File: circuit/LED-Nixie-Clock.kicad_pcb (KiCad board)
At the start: 2 copper layers, 214.6 x 43.2 mm, 197 parts, among them J1 USB Micro, J2 Debug, J3 Boot, SW1 Reset, U1 MCP1700-3302E_SOT23, U2 STM32F103C8Tx, Y1 8MHz, Y2 32.768kHz

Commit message: Improve silk layer labels
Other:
- board text added: "CR2032"
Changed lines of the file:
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@@
   (general
     (thickness 1.6)
-    (drawings 257)
+    (drawings 258)
     (tracks 1823)
     (zones 0)
@@
     (tags "SPST button tactile switch")
     (attr smd)
-    (fp_text reference SW1 (at 0 -2.54 180) (layer B.SilkS)
+    (fp_text reference SW1 (at 0 -2.54 180) (layer B.SilkS) hide
       (effects (font (size 1 1) (thickness 0.15)) (justify mirror))
     )
-    (fp_text value Reset (at 0 -3 180) (layer B.Fab)
+    (fp_text value Reset (at 0 -3 180) (layer B.SilkS)
       (effects (font (size 1 1) (thickness 0.15)) (justify mirror))
     )
@@
     (tags "Keystone type 1058 coin cell retainer")
     (attr smd)
-    (fp_text reference BT1 (at 0 -7.62) (layer B.SilkS)
+    (fp_text reference BT1 (at 0 -7.62) (layer B.SilkS) hide
       (effects (font (size 1 1) (thickness 0.15)) (justify mirror))
     )
@@
       (effects (font (size 1 1) (thickness 0.15)) (justify mirror))
     )
+    (fp_circle (center 0 0) (end 10 0) (layer Dwgs.User) (width 0.15))
+    (fp_arc (start 0 0) (end -10.61275 3.5) (angle -27.4635) (layer B.Fab) (width 0.1))
+    (fp_line (start -7.8026 8) (end 7.8026 8) (layer B.Fab) (width 0.1))
+    (fp_line (start -3.9 -8) (end -7.8026 -8) (layer B.Fab) (width 0.1))
+    (fp_line (start -14.2 3.5) (end -14.2 1.9) (layer B.Fab) (width 0.1))
+    (fp_line (start -14.2 3.5) (end -10.61275 3.5) (layer B.Fab) (width 0.1))
+    (fp_line (start -1.7 -5.8) (end 1.7 -5.8) (layer B.Fab) (width 0.1))
+    (fp_line (start -1.7 -5.8) (end -3.9 -8) (layer B.Fab) (width 0.1))
+    (fp_line (start 1.7 -5.8) (end 3.9 -8) (layer B.Fab) (width 0.1))
+    (fp_line (start 3.9 -8) (end 7.8026 -8) (layer B.Fab) (width 0.1))
+    (fp_line (start -14.2 -3.5) (end -10.61275 -3.5) (layer B.Fab) (width 0.1))
+    (fp_line (start -14.2 -1.9) (end -14.2 -3.5) (layer B.Fab) (width 0.1))
+    (fp_line (start 14.2 3.5) (end 14.2 1.9) (layer B.Fab) (width 0.1))
+    (fp_line (start 10.61275 3.5) (end 14.2 3.5) (layer B.Fab) (width 0.1))
+    (fp_line (start 14.2 -3.5) (end 10.61275 -3.5) (layer B.Fab) (width 0.1))
+    (fp_line (start 14.2 -1.9) (end 14.2 -3.5) (layer B.Fab) (width 0.1))
+    (fp_arc (start 0 0) (end 10.61275 -3.5) (angle -27.4635) (layer B.Fab) (width 0.1))
+    (fp_arc (start 0 0) (end 10.61275 3.5) (angle 27.4635) (layer B.Fab) (width 0.1))
+    (fp_arc (start 0 0) (end -10.61275 -3.5) (angle 27.4635) (layer B.Fab) (width 0.1))
+    (fp_line (start -14.31 3.61) (end -10.692 3.61) (layer B.SilkS) (width 0.12))
+    (fp_line (start -14.31 1.9) (end -14.31 3.61) (layer B.SilkS) (width 0.12))
+    (fp_line (start -7.8473 8.11) (end 7.8473 8.11) (layer B.SilkS) (width 0.12))
+    (fp_line (start 14.31 1.9) (end 14.31 3.61) (layer B.SilkS) (width 0.12))
+    (fp_line (start 10.692 3.61) (end 14.31 3.61) (layer B.SilkS) (width 0.12))
+    (fp_line (start 14.31 -3.61) (end 10.692 -3.61) (layer B.SilkS) (width 0.12))
+    (fp_line (start 14.31 -1.9) (end 14.31 -3.61) (layer B.SilkS) (width 0.12))
+    (fp_line (start 7.8473 -8.11) (end 3.86 -8.11) (layer B.SilkS) (width 0.12))
+    (fp_line (start 1.66 -5.91) (end 3.86 -8.11) (layer B.SilkS) (width 0.12))
+    (fp_line (start 1.66 -5.91) (end -1.66 -5.91) (layer B.SilkS) (width 0.12))
+    (fp_line (start -1.66 -5.91) (end -3.86 -8.11) (layer B.SilkS) (width 0.12))
+    (fp_line (start -3.86 -8.11) (end -7.8473 -8.11) (layer B.SilkS) (width 0.12))
+    (fp_line (start -10.692 -3.61) (end -14.31 -3.61) (layer B.SilkS) (width 0.12))
+    (fp_line (start -14.31 -1.9) (end -14.31 -3.61) (layer B.SilkS) (width 0.12))
+    (fp_arc (start 0 0) (end -10.692 3.61) (angle -27.3) (layer B.SilkS) (width 0.12))
+    (fp_arc (start 0 0) (end 10.692 -3.61) (angle -27.3) (layer B.SilkS) (width 0.12))
+    (fp_arc (start 0 0) (end 10.692 3.61) (angle 27.3) (layer B.SilkS) (width 0.12))
+    (fp_arc (start 0 0) (end -10.692 -3.61) (angle 27.3) (layer B.SilkS) (width 0.12))
+    (fp_line (start -16.45 -4.11) (end -11.06 -4.11) (layer B.CrtYd) (width 0.05))
+    (fp_line (start -16.45 4.11) (end -16.45 -4.11) (layer B.CrtYd) (width 0.05))
+    (fp_line (start -16.45 4.11) (end -11.06 4.11) (layer B.CrtYd) (width 0.05))
+    (fp_line (start 16.45 4.11) (end 11.06 4.11) (layer B.CrtYd) (width 0.05))
+    (fp_line (start 16.45 -4.11) (end 16.45 4.11) (layer B.CrtYd) (width 0.05))
+    (fp_line (start 11.06 -4.11) (end 16.45 -4.11) (layer B.CrtYd) (width 0.05))
+    (fp_arc (start 0 0) (end -11.06 4.11) (angle -139.2) (layer B.CrtYd) (width 0.05))
+    (fp_arc (start 0 0) (end 11.06 -4.11) (angle -139.2) (layer B.CrtYd) (width 0.05))
     (fp_text user %R (at 0 0) (layer B.Fab)
       (effects (font (size 1 1) (thickness 0.15)) (justify mirror))
     )
-    (fp_arc (start 0 0) (end 11.06 -4.11) (angle -139.2) (layer B.CrtYd) (width 0.05))
-    (fp_arc (start 0 0) (end -11.06 4.11) (angle -139.2) (layer B.CrtYd) (width 0.05))
-    (fp_line (start 11.06 -4.11) (end 16.45 -4.11) (layer B.CrtYd) (width 0.05))
-    (fp_line (start 16.45 -4.11) (end 16.45 4.11) (layer B.CrtYd) (width 0.05))
-    (fp_line (start 16.45 4.11) (end 11.06 4.11) (layer B.CrtYd) (width 0.05))
-    (fp_line (start -16.45 4.11) (end -11.06 4.11) (layer B.CrtYd) (width 0.05))
-    (fp_line (start -16.45 4.11) (end -16.45 -4.11) (layer B.CrtYd) (width 0.05))
-    (fp_line (start -16.45 -4.11) (end -11.06 -4.11) (layer B.CrtYd) (width 0.05))
-    (fp_arc (start 0 0) (end -10.692 -3.61) (angle 27.3) (layer B.SilkS) (width 0.12))
-    (fp_arc (start 0 0) (end 10.692 3.61) (angle 27.3) (layer B.SilkS) (width 0.12))
-    (fp_arc (start 0 0) (end 10.692 -3.61) (angle -27.3) (layer B.SilkS) (width 0.12))
-    (fp_arc (start 0 0) (end -10.692 3.61) (angle -27.3) (layer B.SilkS) (width 0.12))
-    (fp_line (start -14.31 -1.9) (end -14.31 -3.61) (layer B.SilkS) (width 0.12))
-    (fp_line (start -10.692 -3.61) (end -14.31 -3.61) (layer B.SilkS) (width 0.12))
-    (fp_line (start -3.86 -8.11) (end -7.8473 -8.11) (layer B.SilkS) (width 0.12))
-    (fp_line (start -1.66 -5.91) (end -3.86 -8.11) (layer B.SilkS) (width 0.12))
-    (fp_line (start 1.66 -5.91) (end -1.66 -5.91) (layer B.SilkS) (width 0.12))
-    (fp_line (start 1.66 -5.91) (end 3.86 -8.11) (layer B.SilkS) (width 0.12))
-    (fp_line (start 7.8473 -8.11) (end 3.86 -8.11) (layer B.SilkS) (width 0.12))
-    (fp_line (start 14.31 -1.9) (end 14.31 -3.61) (layer B.SilkS) (width 0.12))
-    (fp_line (start 14.31 -3.61) (end 10.692 -3.61) (layer B.SilkS) (width 0.12))
-    (fp_line (start 10.692 3.61) (end 14.31 3.61) (layer B.SilkS) (width 0.12))
-    (fp_line (start 14.31 1.9) (end 14.31 3.61) (layer B.SilkS) (width 0.12))
-    (fp_line (start -7.8473 8.11) (end 7.8473 8.11) (layer B.SilkS) (width 0.12))
-    (fp_line (start -14.31 1.9) (end -14.31 3.61) (layer B.SilkS) (width 0.12))
-    (fp_line (start -14.31 3.61) (end -10.692 3.61) (layer B.SilkS) (width 0.12))
-    (fp_arc (start 0 0) (end -10.61275 -3.5) (angle 27.4635) (layer B.Fab) (width 0.1))
-    (fp_arc (start 0 0) (end 10.61275 3.5) (angle 27.4635) (layer B.Fab) (width 0.1))
-    (fp_arc (start 0 0) (end 10.61275 -3.5) (angle -27.4635) (layer B.Fab) (width 0.1))
-    (fp_line (start 14.2 -1.9) (end 14.2 -3.5) (layer B.Fab) (width 0.1))
-    (fp_line (start 14.2 -3.5) (end 10.61275 -3.5) (layer B.Fab) (width 0.1))
-    (fp_line (start 10.61275 3.5) (end 14.2 3.5) (layer B.Fab) (width 0.1))
-    (fp_line (start 14.2 3.5) (end 14.2 1.9) (layer B.Fab) (width 0.1))
-    (fp_line (start -14.2 -1.9) (end -14.2 -3.5) (layer B.Fab) (width 0.1))
-    (fp_line (start -14.2 -3.5) (end -10.61275 -3.5) (layer B.Fab) (width 0.1))
-    (fp_line (start 3.9 -8) (end 7.8026 -8) (layer B.Fab) (width 0.1))
-    (fp_line (start 1.7 -5.8) (end 3.9 -8) (layer B.Fab) (width 0.1))
-    (fp_line (start -1.7 -5.8) (end -3.9 -8) (layer B.Fab) (width 0.1))
-    (fp_line (start -1.7 -5.8) (end 1.7 -5.8) (layer B.Fab) (width 0.1))
-    (fp_line (start -14.2 3.5) (end -10.61275 3.5) (layer B.Fab) (width 0.1))
-    (fp_line (start -14.2 3.5) (end -14.2 1.9) (layer B.Fab) (width 0.1))
-    (fp_line (start -3.9 -8) (end -7.8026 -8) (layer B.Fab) (width 0.1))
-    (fp_line (start -7.8026 8) (end 7.8026 8) (layer B.Fab) (width 0.1))
-    (fp_arc (start 0 0) (end -10.61275 3.5) (angle -27.4635) (layer B.Fab) (width 0.1))
-    (fp_circle (center 0 0) (end 10 0) (layer Dwgs.User) (width 0.15))
-    (pad 1 smd rect (at -14.68 0) (size 2.54 3.51) (layers B.Cu B.Paste B.Mask)
-      (net 56 "Net-(BT1-Pad1)"))
     (pad 2 smd rect (at 14.68 0) (size 2.54 3.51) (layers B.Cu B.Paste B.Mask)
       (net 1 GND))
+    (pad 1 smd rect (at -14.68 0) (size 2.54 3.51) (layers B.Cu B.Paste B.Mask)
+      (net 56 "Net-(BT1-Pad1)"))
     (model ${KISYS3DMOD}/Battery.3dshapes/BatteryHolder_Keystone_1058_1x2032.wrl
       (at (xyz 0 0 0))
@@
     (tags "Surface mounted pin header SMD 2x05 1.27mm double row")
     (attr smd)
-    (fp_text reference J2 (at 0 -4.445 180) (layer B.SilkS)
+    (fp_text reference J2 (at 0 -4.445 180) (layer B.SilkS) hide
       (effects (font (size 1 1) (thickness 0.15)) (justify mirror))
     )
-    (fp_text value Debug (at 0 -4.235 180) (layer B.Fab)
+    (fp_text value Debug (at 0 -4.235 180) (layer B.SilkS)
       (effects (font (size 1 1) (thickness 0.15)) (justify mirror))
     )
@@
     )
   )
+  (gr_text CR2032 (at 180.975 97.155) (layer B.SilkS)
+    (effects (font (size 1 1) (thickness 0.15)) (justify mirror))
+  )
   (gr_line (start 143.8275 90.3605) (end 146.8755 90.3605) (layer Dwgs.User) (width 0.1))

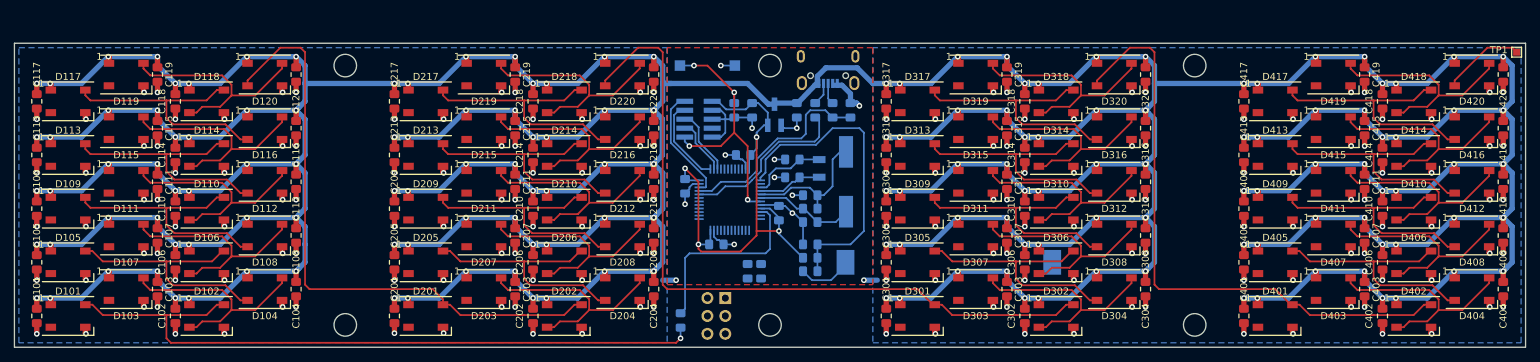
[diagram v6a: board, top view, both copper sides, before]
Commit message: Add serial port and replace reset with a boot select pushbutton
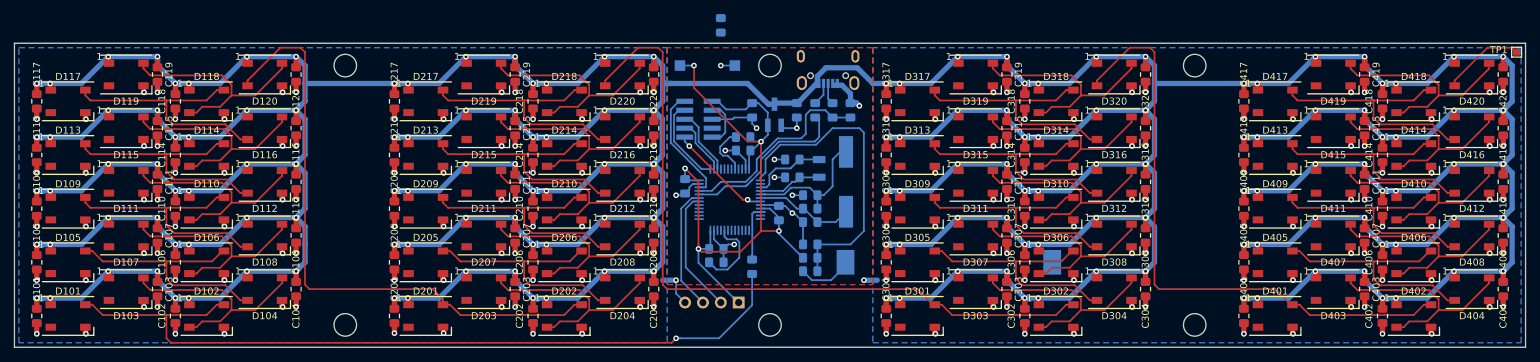
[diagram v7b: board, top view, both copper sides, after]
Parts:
- removed C14: 100n, Capacitor_SMD:C_0805_2012Metric_Pad1.15x1.40mm_HandSolder
- added R7: 10k, Resistor_SMD:R_0805_2012Metric_Pad1.15x1.40mm_HandSolder, B.Cu at (148.0, 105.4)
- J3: value Boot -> Serial; footprint Connector_PinHeader_2.54mm:PinHeader_2x03_P2.54mm_Vertical -> Connector_PinHeader_2.54mm:PinHeader_1x04_P2.54mm_Vertical
- SW1: value Reset -> Boot0
- moved R6 35.1 mm to (148.6, 71.8)
- moved R5 19.2 mm to (151.8, 87.6), turned to 0 degrees
- moved R8 12.7 mm to (153.0, 106.0)
- moved J3 2.01 mm to (151.1, 111.1), turned to 90 degrees
- moved C9 0.64 mm to (151.8, 89.5)
- moved C7 0.63 mm to (148.0, 103.5)
- renumbered R7 to R8
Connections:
- J3 pad 2: VDD -> /USART1_TX
- J3 pad 3: Net-(J3-Pad3) -> /USART1_RX
- J3 pad 4: Net-(J3-Pad4) -> GND
- R5 pad 1: Net-(J3-Pad3) -> /BOOT0
- R5 pad 2: /BOOT0 -> Net-(R5-Pad2)
- R6 pad 1: /BOOT1 -> GND
- R6 pad 2: Net-(J3-Pad4) -> Net-(R5-Pad2)
- SW1 pad 1: GND -> Net-(R5-Pad2)
- SW1 pad 2: /RESET -> VDD
- U2 pad 30: (no net) -> /USART1_TX
- U2 pad 31: (no net) -> /USART1_RX
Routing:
- net VDD: track 75.0 -> 102.4 mm, vias 4 -> 5
- net /RESET: track 37.5 -> 14.9 mm, vias 4 -> 2
- net Net-(R8-Pad2): track 27.9 -> 8.60 mm
- net /USART1_RX: track 0.00 -> 17.8 mm
- net /USART1_TX: track 0.00 -> 17.7 mm
- net /Digit 1/DIN: track 99.0 -> 114.3 mm
- net /BOOT1: track 0.00 -> 11.0 mm
- net /BOOT0: track 0.00 -> 7.26 mm
- net GND: track 255.8 -> 260.8 mm, vias 173 -> 172
- net Net-(R5-Pad2): track 0.00 -> 2.00 mm, vias 0 -> 1
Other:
- board text added: "3.3V"
- board text added: "GND"
- board text added: "Rx"
- board text added: "Tx"

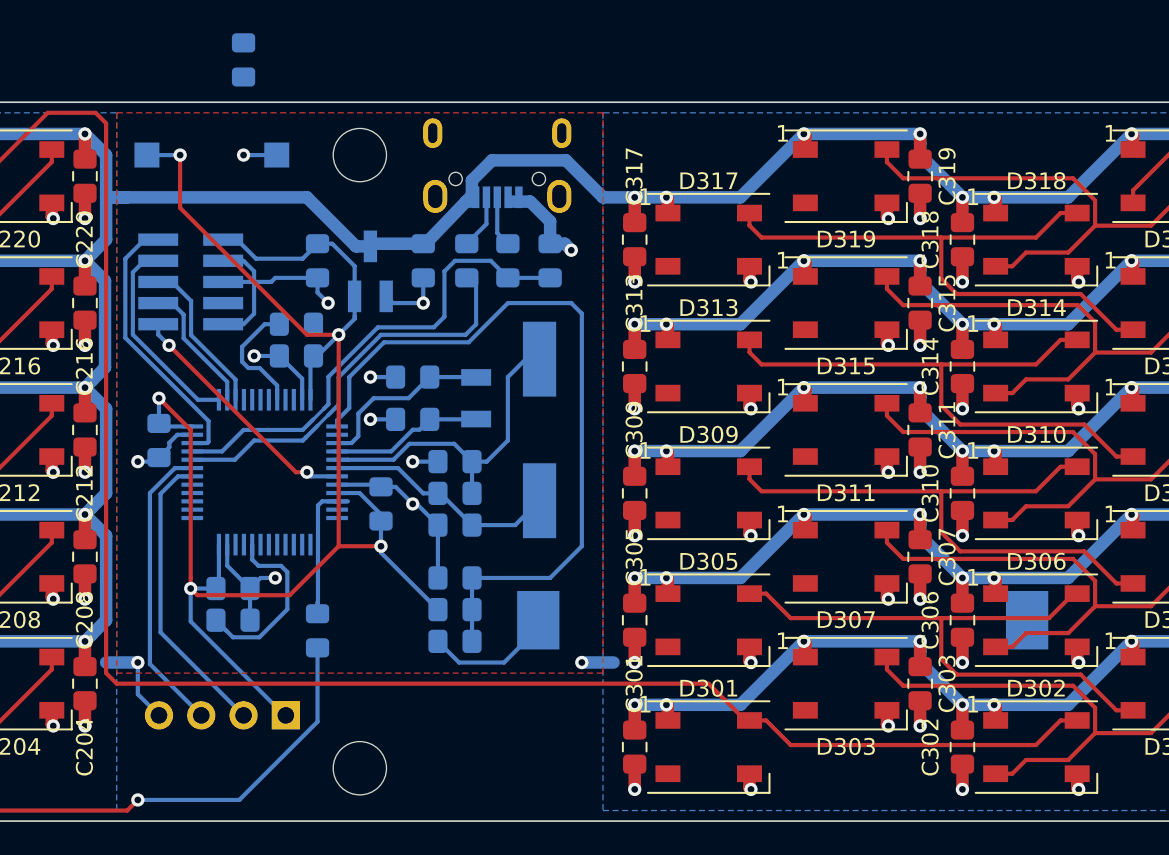
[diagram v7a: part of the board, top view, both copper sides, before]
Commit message: Reroute PCB traces for more compact layout and 5032 crystal
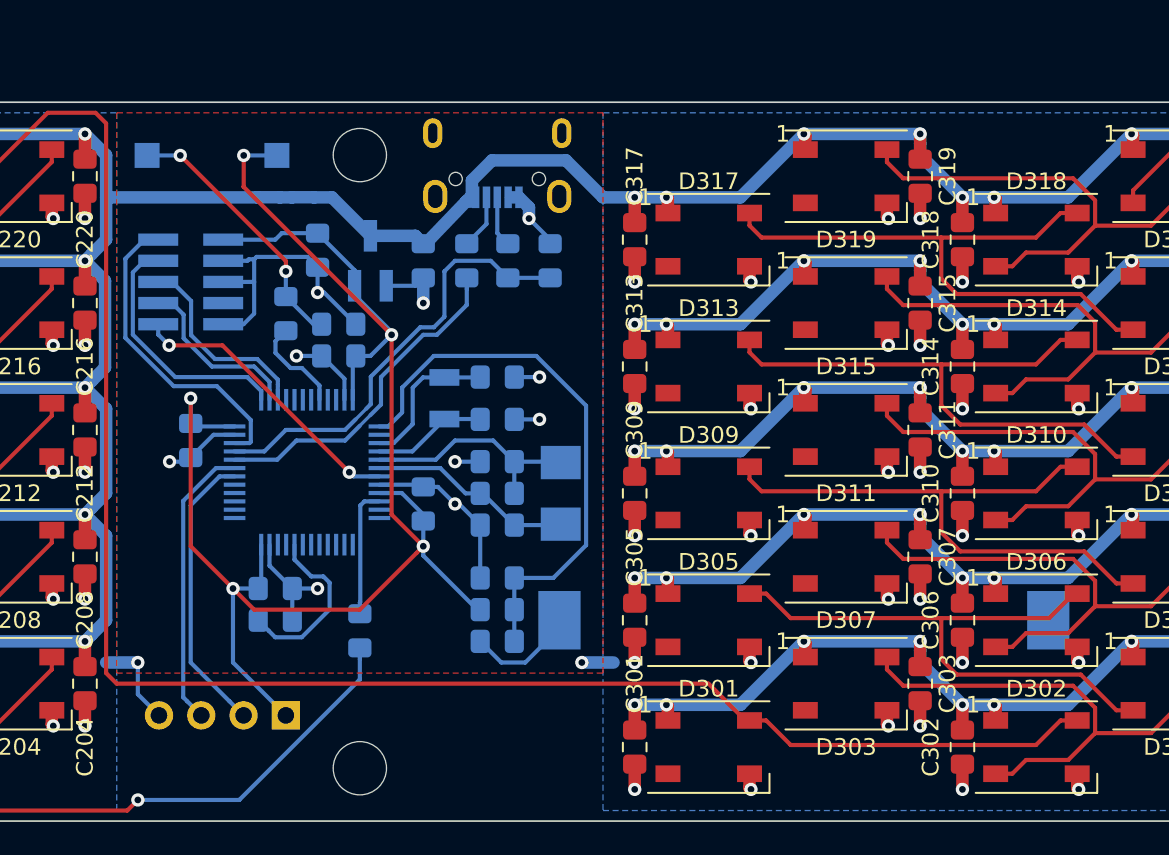
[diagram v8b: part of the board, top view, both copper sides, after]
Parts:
- Y1: footprint Crystal:Crystal_SMD_HC49-SD -> Crystal:Crystal_SMD_5032-2Pin_5.0x3.2mm
- moved R6 16.9 mm to (154.3, 87.6), turned to 180 degrees
- moved C12 5.08 mm to (163.8, 90.8), turned to 0 degrees
- moved C13 5.08 mm to (163.8, 93.3), turned to 0 degrees
- moved Y1 4.02 mm to (167.6, 97.8)
- moved C10 2.54 mm to (163.8, 95.9)
- moved C11 2.54 mm to (163.8, 99.7)
- moved C5 2.54 mm to (163.8, 102.9)
- moved C9 2.54 mm to (154.3, 89.5)
- moved D1 2.54 mm to (163.8, 106.7)
- moved D2 2.54 mm to (163.8, 104.8)
- moved R4 2.54 mm to (163.8, 97.8)
- moved C6 2.54 mm to (159.4, 98.4)
- moved C7 2.54 mm to (150.5, 103.5)
- moved R7 2.54 mm to (150.5, 105.4)
- moved R8 2.54 mm to (155.6, 106.0)
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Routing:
- net Net-(R5-Pad2): track 2.00 -> 15.9 mm, vias 1 -> 2
- net +BATT: track 44.5 -> 33.6 mm
- net /OSC_IN: track 20.1 -> 13.8 mm
- net /USBDM: track 24.2 -> 20.4 mm
- net /OSC32_OUT: track 9.97 -> 6.88 mm
- net /SWCLK-JTCK: track 12.3 -> 15.2 mm
- net GND: track 260.8 -> 263.6 mm
- net /SWDIO-JTMS: track 16.5 -> 19.1 mm
- net /USBDP: track 28.6 -> 26.1 mm
- net /RESET: track 14.9 -> 17.4 mm
- net /JTDI: track 8.01 -> 10.6 mm
- net /SWO-JTDO: track 9.49 -> 12.0 mm
- net /OSC32_IN: track 11.4 -> 8.98 mm
- net /OSC_OUT: track 14.6 -> 12.3 mm
- net VBUS: track 1247.9 -> 1246.5 mm
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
